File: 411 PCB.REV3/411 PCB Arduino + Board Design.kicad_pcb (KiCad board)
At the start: 2 copper layers, 42.1 x 62.6 mm, 30 parts, among them J1 ICSP CONN, J2 Conn_01x06_MountingPin, J4 Conn_01x04, Q1 Q_NMOS_GDS, SW1 SW_SPST, SW3 SW_MEC_5E, U1 ATmega328P-P, Y1 8 MHz

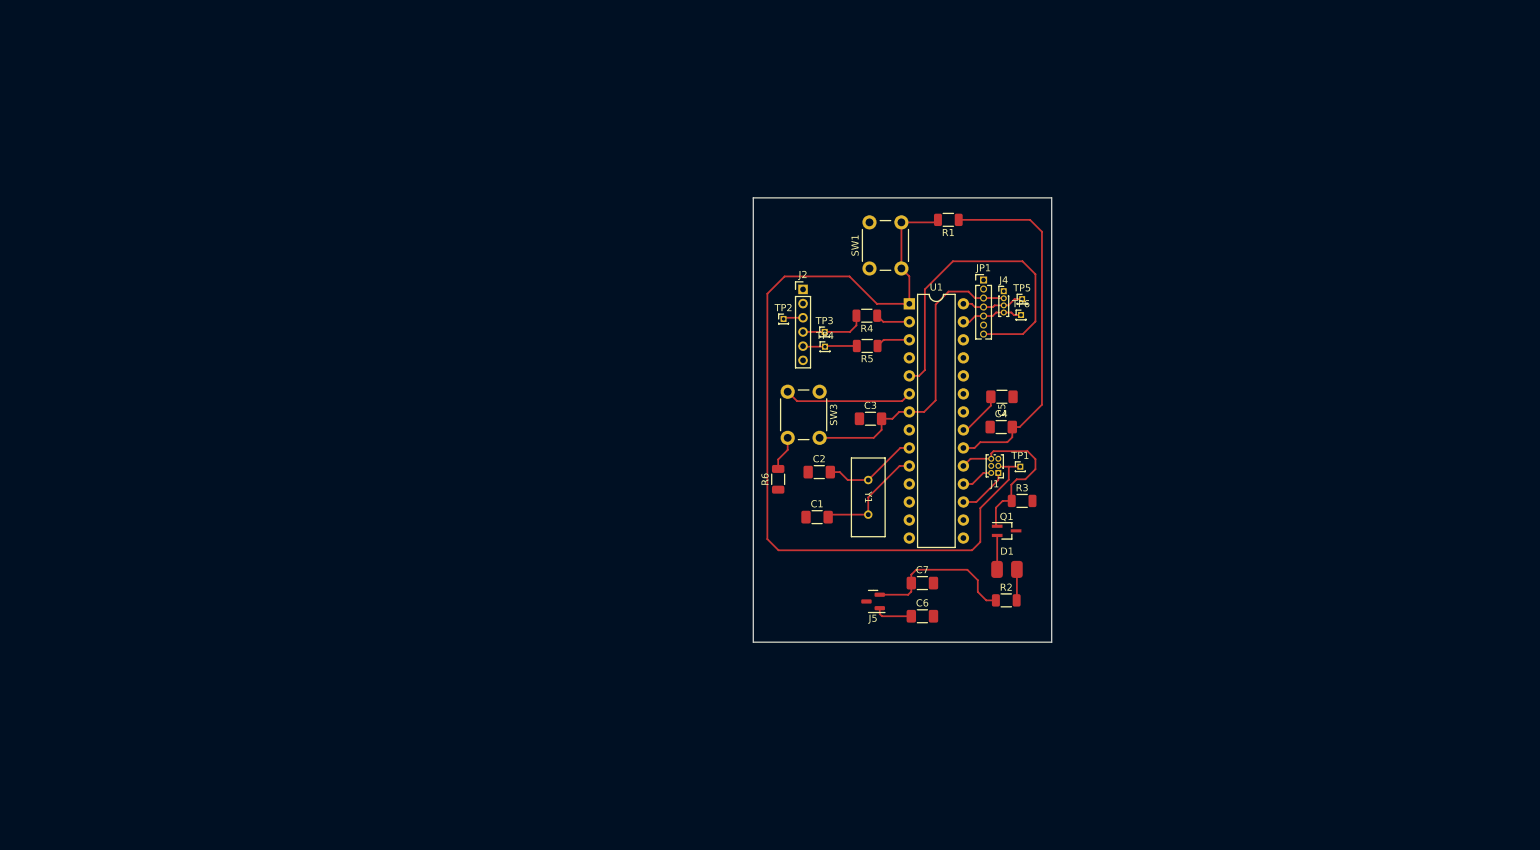
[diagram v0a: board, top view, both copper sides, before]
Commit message: Rev4 Fixed Footprint and Schematic Layout a bit.
Monday 11/13/2023 Will do the PCB final routing
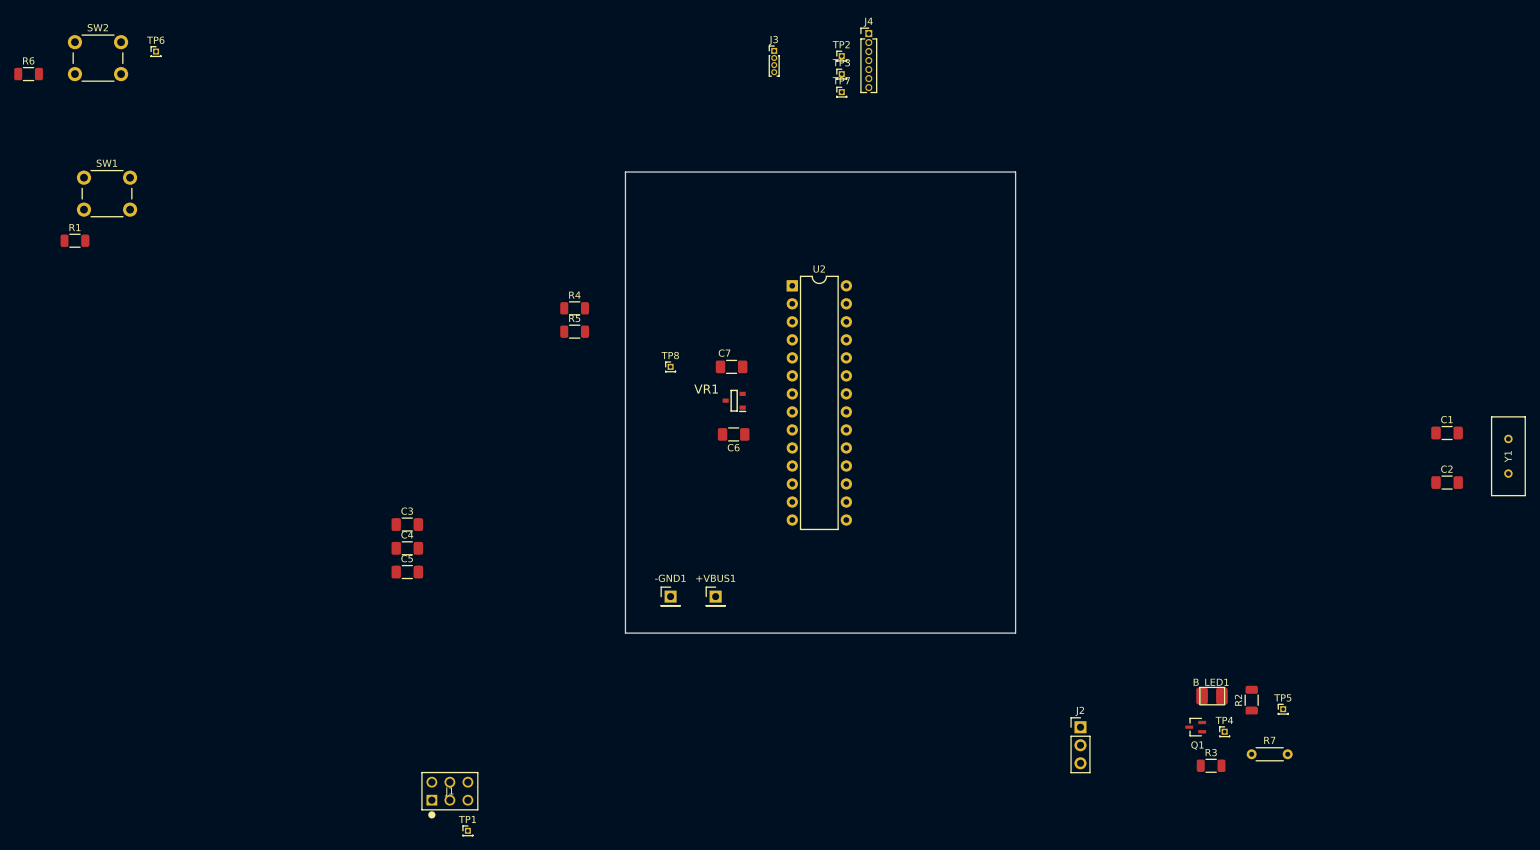
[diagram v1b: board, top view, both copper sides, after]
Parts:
- removed D1: LED (100mA Max), LED_SMD:LED_0805_2012Metric_Pad1.15x1.40mm_HandSolder
- removed J5: ~, Package_TO_SOT_SMD:SOT-23
- removed JP1: HEADER-1X770MIL, Connector_PinHeader_1.27mm:PinHeader_1x07_P1.27mm_Vertical
- removed SW3: SW_MEC_5E, Button_Switch_THT:SW_PUSH_6mm
- removed U1: ATmega328P-P, Package_DIP:DIP-28_W7.62mm
- added +VBUS1: Conn_01x01_Pin, Connector_PinHeader_2.54mm:PinHeader_1x01_P2.54mm_Vertical, F.Cu at (132.7, 109.9)
- added -GND1: Conn_01x01_Pin, Connector_PinHeader_2.54mm:PinHeader_1x01_P2.54mm_Vertical, F.Cu at (126.4, 109.9)
- added B_LED1: LED (100mA Max), LED_SMD:LTST-B680, F.Cu at (202.6, 123.8)
- added J3: Conn_01x04, Connector_PinHeader_1.00mm:PinHeader_1x04_P1.00mm_Vertical, F.Cu at (141.0, 32.9)
- added R7: 0 Ohm, Resistor_THT:R_Axial_DIN0204_L3.6mm_D1.6mm_P5.08mm_Horizontal, F.Cu at (208.3, 132.1)
- added SW2: SW_MEC_5E, Button_Switch_THT:SW_PUSH_6mm, F.Cu at (42.4, 31.7)
- added TP7: TestPoint, Connector_PinHeader_1.00mm:PinHeader_1x01_P1.00mm_Vertical, F.Cu at (150.5, 38.7)
- added TP8: TestPoint, Connector_PinHeader_1.00mm:PinHeader_1x01_P1.00mm_Vertical, F.Cu at (126.4, 77.5)
- added U2: ATmega328P-P, Package_DIP:DIP-28_W7.62mm, F.Cu at (143.5, 66.0)
- added VR1: ~, SamacSys_Parts:SOT96P240X120-3N, F.Cu at (135.3, 82.2)
- J1: footprint Connector_PinHeader_1.00mm:PinHeader_2x03_P1.00mm_Vertical -> PH2_06_UA:CONN_PH2-06-UA_ADM
- J2: value Conn_01x06_MountingPin -> ~; footprint Connector_PinHeader_2.00mm:PinHeader_1x06_P2.00mm_Vertical -> Connector_PinHeader_2.54mm:PinHeader_1x03_P2.54mm_Vertical
- J4: value Conn_01x04 -> HEADER-1X770MIL; footprint Connector_PinHeader_1.00mm:PinHeader_1x04_P1.00mm_Vertical -> Connector_PinHeader_1.27mm:PinHeader_1x07_P1.27mm_Vertical
- Q1: footprint Package_TO_SOT_SMD:SOT-323_SC-70_Handsoldering -> DMN63D9LW:SOIC_D8LW-13_DIO
- moved TP6 127.5 mm to (53.8, 33.0)
- moved R1 123.2 mm to (42.4, 59.7), turned to 0 degrees
- moved R6 120.1 mm to (35.9, 36.2), turned to 0 degrees
- moved SW1 111.5 mm to (43.7, 50.8), turned to 0 degrees
- moved TP1 93.3 mm to (97.8, 142.9)
- moved J1 92.2 mm to (92.7, 138.6), turned to 0 degrees
- moved Y1 90.3 mm to (244.5, 92.5), turned to 90 degrees
- moved C1 89.6 mm to (235.8, 86.8)
- moved C2 88.5 mm to (235.8, 93.8)
- moved C5 87.4 mm to (89.2, 106.4), turned to 0 degrees
- moved C4 85.5 mm to (89.2, 103.0)
- moved TP4 78.2 mm to (204.5, 128.9)
- moved J2 73.1 mm to (184.2, 128.3)
- moved TP5 68.5 mm to (212.7, 125.7)
- moved C3 67.0 mm to (89.2, 99.7)
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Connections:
- C4 pad 1: GND -> Net-(U2-AREF)
- C4 pad 2: +3.3V -> Net-(C4-Pad2)
- C5 pad 1: GND -> +3.3V
- C5 pad 2: Net-(U1-AREF) -> Net-(C4-Pad2)
- C6 pad 1: +VDC -> VBUS
- J2 pad 1: GND -> Net-(J2-Pin_1)
- J2 pad 2: unconnected-(J2-Pin_2-Pad2) -> Net-(J2-Pin_2)
- J2 pad 3: Net-(J2-Pin_3) -> GND
- J4 pad 1: GND -> /V_IN
- J4 pad 2: +3.3V -> GND
- J4 pad 3: /SCL_3.3V -> +3.3V
- J4 pad 4: /SDA_3.3V -> /SCL_3.3V
- Q1 pad 1: Net-(J1-SCK) -> Net-(Q1-G)
- R3 pad 1: Net-(J1-SCK) -> Net-(Q1-G)
- R4 pad 2: Net-(J2-Pin_4) -> Net-(J2-Pin_1)
- R5 pad 2: Net-(J2-Pin_5) -> Net-(J2-Pin_2)
- TP2 pad 1: Net-(J2-Pin_3) -> /SCL_3.3V
- TP3 pad 1: Net-(J2-Pin_4) -> /SDA_3.3V
- TP4 pad 1: Net-(J2-Pin_5) -> Net-(J1-SCK)
- TP5 pad 1: /SCL_3.3V -> +3.3V
- TP6 pad 1: /SDA_3.3V -> Net-(SW2-A)
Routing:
- net Net-(J1-~{RST}): track 121.0 -> 0.00 mm
- net +3.3V: track 117.0 -> 0.00 mm
- net /LED_EN: track 46.6 -> 0.00 mm
- net Net-(J1-SCK): track 25.3 -> 0.00 mm
- net Net-(SW3-A): track 18.1 -> 0.00 mm
- net Net-(U2-XTAL1/PB6): track 15.9 -> 0.00 mm
- net Net-(U2-XTAL2/PB7): track 13.5 -> 0.00 mm
- net Net-(J2-Pin_4): track 9.28 -> 0.00 mm
- net /SCL_3.3V: track 8.93 -> 0.00 mm
- net /SDA_3.3V: track 8.82 -> 0.01 mm
- net Net-(J2-Pin_5): track 7.65 -> 0.00 mm
- net Net-(J1-MOSI): track 7.21 -> 0.00 mm
- net Net-(U1-AREF): track 6.55 -> 0.00 mm
- net +VDC: track 5.40 -> 0.00 mm
- net Net-(R6-Pad2): track 4.94 -> 0.00 mm
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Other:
- board size 42.1 x 62.6 mm -> 55 x 65 mm

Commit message: 411 PCB Rev4+ Updated and Routed Layout
This is the pre submission board. Before Ben check
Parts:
- J3: footprint Connector_PinHeader_1.00mm:PinHeader_1x04_P1.00mm_Vertical -> Connector_PinHeader_2.54mm:PinHeader_1x04_P2.54mm_Vertical
- J4: footprint Connector_PinHeader_1.27mm:PinHeader_1x07_P1.27mm_Vertical -> Connector_PinHeader_2.54mm:PinHeader_1x07_P2.54mm_Vertical
- LED1: renamed from B_LED1; value LED (100mA Max) -> Blue LED (100mA Max)
- SW2: footprint Button_Switch_THT:SW_PUSH_6mm -> Connector_PinHeader_2.54mm:PinHeader_1x04_P2.54mm_Vertical
- moved Y1 106.7 mm to (137.9, 99.0)
- moved R6 105.4 mm to (133.2, 76.6), turned to 90 degrees
- moved C1 104.1 mm to (131.9, 93.5)
- moved C2 104.0 mm to (131.9, 99.2)
- moved R1 96.0 mm to (137.9, 69.0), turned to 90 degrees
- moved SW2 95.9 mm to (129.2, 72.5)
- moved TP6 90.8 mm to (129.2, 83.7)
- moved SW1 87.8 mm to (129.7, 67.9), turned to 90 degrees
- moved C5 77.7 mm to (164.2, 85.7), turned to 180 degrees
- moved C4 72.1 mm to (159.1, 85.2), turned to 90 degrees
- moved J1 65.7 mm to (150.5, 107.3), turned to 180 degrees
- moved TP5 59.1 mm to (169.3, 85.7)
- moved R7 56.5 mm to (162.2, 99.4), turned to 90 degrees
- moved TP1 56.1 mm to (141.4, 107.6)
- moved R3 55.2 mm to (158.1, 100.9), turned to -90 degrees
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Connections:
- net /SCL_3.3V renamed /SDA-
- net /SDA_3.3V renamed /SDA+
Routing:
- net +3.3V: track 0.00 -> 97.2 mm, vias 0 -> 4
- net Net-(J1-~{RST}): track 0.00 -> 79.0 mm
- net Net-(U2-(RXD)PD0): track 0.00 -> 67.4 mm, vias 0 -> 1
- net Net-(U2-(TXD)PD1): track 0.00 -> 62.8 mm, vias 0 -> 1
- net Net-(J1-SCK): track 0.00 -> 37.0 mm, vias 0 -> 2
- net VBUS: track 0.00 -> 27.8 mm
- net Net-(J1-MOSI): track 0.00 -> 25.7 mm
- net Net-(U2-XTAL+): track 0.00 -> 18.9 mm
- net Net-(SW2-A): track 0.00 -> 18.0 mm, vias 0 -> 1
- net Net-(U2-XTAL-): track 0.00 -> 17.1 mm
- net /SDA+: track 0.01 -> 17.0 mm
- net /SDA-: track 0.00 -> 17.0 mm
- net Net-(J1-MISO): track 0.00 -> 16.4 mm
- net Net-(C4-Pad2): track 0.00 -> 14.1 mm
- net /LED_EN: track 0.00 -> 11.0 mm
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- added copper zone on B.Cu, net GND
- added copper zone on F.Cu, net GND
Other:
- board size 55 x 65 mm -> 55 x 60 mm
- rule pad_to_mask_clearance: 0 -> 0.0508
